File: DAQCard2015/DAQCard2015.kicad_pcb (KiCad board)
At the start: 4 copper layers, 160 x 160 mm, 197 parts, among them CON1 BARREL_JACK, P1 QTH-090-01-F-D-A, P2 QTH-090-01-F-D-A, P3 miniDIL20, P4 LEMO_EPY.00.250.NTN, P5 LEMO_EPY.00.250.NTN, P6 FAN, P7 CONN_02X20_Double, Q1 Q_NPN_BCE, SW1 SPST, U1 RJ45x8, U10 AD9219, U11 THS4524IDBTR, U12 AD9219, U13 THS4524IDBTR, U14 AD9219, U15 THS4524IDBTR, U16 AD9219, U17 THS4524IDBTR, U18 AD9219, U19 CDBHD240-G, U2 AD5628, U20 LM1086, U21 APXS002A0X-SRZ, U22 APXS002A0X-SRZ, U23 APXS002A0X-SRZ, U24 MCP65R41, U3 THS4524IDBTR, U4 AD9219, U5 THS4524IDBTR, U6 AD9219, U7 THS4524IDBTR, U8 AD9219, U9 THS4524IDBTR

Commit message: Various updates to DAQ board focusing on power system
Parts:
- removed C60, C61: 10uF, Capacitors_SMD:C_0805
- removed C62, C63: 10000pF, Capacitors_SMD:C_0603
- removed C64: 3900pF, Capacitors_SMD:C_0603
- removed C65, C66, C67, C68, C69: 47uF, extras:SMD_Cap_8mmDia
- removed REF** (x4): MountingHole_2-5mm, Mounting_Holes:MountingHole_2-5mm
- removed U19: CDBHD240-G, extras:mini-DIP4
- removed U22, U23: APXS002A0X-SRZ, extras:APXS002A0X-SRZ
- added C70: 22nF, Capacitors_SMD:C_1812, F.Cu at (54.1, 150.8)
- added D2: D, Diodes_SMD:SMA_Standard, F.Cu at (51.2, 159.3)
- added D4: MBRA340, Diodes_SMD:SMA_Standard, F.Cu at (151.8, 157.5)
- added DB1: NMLU1210, extras:NMLU1210, F.Cu at (152.8, 167.4)
- added K1: 1462042-8, extras:1462042-8, F.Cu at (54.4, 160.4)
- added L1: 5.6uH, extras:SLF101, F.Cu at (138.8, 152.3)
- added P9: SHV, extras:TE_1217133-1, F.Cu at (58.0, 160.8)
- added Q2: NPN, Housings_SOT-23_SOT-143_TSOT-6:SOT-23, F.Cu at (59.3, 162.7)
- C53: value 100uF -> 22uF
- C55: value 10uF -> 680pF; footprint Capacitors_SMD:C_0805 -> Capacitors_SMD:C_0603
- C56: value 100uF -> 0.47uF; footprint extras:SMD_Cap_8mmDia -> Capacitors_SMD:C_0603
- C57: value 100uF -> 47uF
- C58: value 100uF -> 10uF; footprint extras:SMD_Cap_8mmDia -> Capacitors_SMD:C_0805
- C59: value 10uF -> .1uF; footprint Capacitors_SMD:C_0805 -> Capacitors_SMD:C_0603
- D1: value LED -> Dialight_5690101372F; footprint LEDs:LED-1206 -> extras:Dialight_5690101372F
- R46: value 150R -> 63.4k
- R47: value 5k -> 15k
- R48: value 150R -> 100k
- R49: value 5k -> 536k
- R50: value 220R -> R
- R51: value 2.22k -> R
- R52: value 150R -> R
- R57, R58, R59, R60: footprint Resistors_SMD:R_0603 -> Resistors_SMD:R_1206
- SW1: value SPST -> DPDT
- U11, U13, U15, U17, U3, U5, U7, U9: footprint Housings_SSOP:TSSOP-38_4.4x9.7mm_Pitch0.5mm -> extras:TSSOP-38_4.4x9.7mm_Pitch0.5mm
- U2: footprint Housings_SSOP:TSSOP-16_4.4x5mm_Pitch0.65mm -> extras:TSSOP-16_4.4x5mm_Pitch0.65mm
- U21: value APXS002A0X-SRZ -> LT1913; footprint extras:APXS002A0X-SRZ -> extras:LT1913
- moved R2 282.4 mm to (23.1, 79.9), turned to 270 degrees
- moved R5 276.5 mm to (23.5, 115.8), turned to 270 degrees
- moved R1 265.8 mm to (25.3, 79.9), turned to 90 degrees
- moved C3 263.2 mm to (24.3, 76.9), turned to 180 degrees
- moved C2 256.9 mm to (24.2, 82.9), turned to 180 degrees
- moved C1 249.9 mm to (24.1, 85.7), turned to 180 degrees
- moved R52 235.1 mm to (50.2, 172.4)
- moved D1 231.9 mm to (44.7, 174.3), turned to 180 degrees
- moved R51 199.6 mm to (49.1, 181.5)
- moved R50 194.1 mm to (50.0, 175.3)
- moved R4 189.7 mm to (26.4, 114.4)
- moved C4 180.2 mm to (26.5, 117.3)
- moved C55 142.8 mm to (144.8, 141.5), turned to 180 degrees
- moved C53 142.1 mm to (143.6, 165.6)
- moved RV1 127.4 mm to (157.3, 120.0), turned to 90 degrees
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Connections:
- C55 pad 1: 5Vdig -> Net-(C55-Pad1)
- C56 pad 1: 5Vdig -> Net-(C56-Pad1)
- C56 pad 2: GNDdig -> Net-(C56-Pad2)
- C57 pad 2: GNDdig -> GND
- C58 pad 1: 5Vdig -> 1V8ana
- C58 pad 2: GNDdig -> GND
- C59 pad 1: 5Vdig -> 1V8ana
- C59 pad 2: GNDdig -> GND
- CON1 pad 1: Net-(CON1-Pad1) -> (no net)
- P1 pad 101: /ZEM4310/+3.3VDD -> 3V3dig
- P1 pad 107: /ZEM4310/+3.3VDD -> 3V3dig
- P1 pad 113: /ZEM4310/+3.3VDD -> 3V3dig
- P1 pad 119: /ZEM4310/+3.3VDD -> 3V3dig
- P1 pad 12: (no net) -> 1V8dig
- P1 pad 125: /ZEM4310/+3.3VDD -> 3V3dig
- P1 pad 131: /ZEM4310/+3.3VDD -> 3V3dig
- P1 pad 137: /ZEM4310/+3.3VDD -> 3V3dig
- P1 pad 143: /ZEM4310/+3.3VDD -> 3V3dig
- P1 pad 149: /ZEM4310/+3.3VDD -> 3V3dig
- P1 pad 155: /ZEM4310/+3.3VDD -> 3V3dig
- P1 pad 161: /ZEM4310/+3.3VDD -> 3V3dig
- P1 pad 167: /ZEM4310/+3.3VDD -> 3V3dig
- P1 pad 173: /ZEM4310/+3.3VDD -> 3V3dig
- P1 pad 179: /ZEM4310/+3.3VDD -> 3V3dig
- P1 pad 180: /ZEM4310/PRSNTn -> GND
- P1 pad 65: /ZEM4310/+3.3VDD -> 3V3dig
- P1 pad 71: /ZEM4310/+3.3VDD -> 3V3dig
- P1 pad 77: /ZEM4310/+3.3VDD -> 3V3dig
- P1 pad 83: /ZEM4310/+3.3VDD -> 3V3dig
- P1 pad 89: /ZEM4310/+3.3VDD -> 3V3dig
- P1 pad 95: /ZEM4310/+3.3VDD -> 3V3dig
- P2 pad 101: /ZEM4310/+3.3VDD -> 3V3dig
- P2 pad 107: /ZEM4310/+3.3VDD -> 3V3dig
- P2 pad 11: /ZEM4310/+VDC -> 5Vdig
- P2 pad 113: /ZEM4310/+3.3VDD -> 3V3dig
- P2 pad 119: /ZEM4310/+3.3VDD -> 3V3dig
- P2 pad 12: /ZEM4310/+VDC -> 5Vdig
- P2 pad 125: /ZEM4310/+3.3VDD -> 3V3dig
- P2 pad 131: /ZEM4310/+3.3VDD -> 3V3dig
- P2 pad 137: /ZEM4310/+3.3VDD -> 3V3dig
- P2 pad 143: /ZEM4310/+3.3VDD -> 3V3dig
- P2 pad 149: /ZEM4310/+3.3VDD -> 3V3dig
- P2 pad 155: /ZEM4310/+3.3VDD -> 3V3dig
- P2 pad 161: /ZEM4310/+3.3VDD -> 3V3dig
- P2 pad 167: /ZEM4310/+3.3VDD -> 3V3dig
- P2 pad 173: /ZEM4310/+3.3VDD -> 3V3dig
- P2 pad 179: /ZEM4310/+3.3VDD -> 3V3dig
- P2 pad 180: /ZEM4310/PRSNTn -> GND
- P2 pad 5: /ZEM4310/+VDC -> 5Vdig
- P2 pad 6: /ZEM4310/+VDC -> 5Vdig
- P2 pad 65: /ZEM4310/+3.3VDD -> 3V3dig
- P2 pad 71: /ZEM4310/+3.3VDD -> 3V3dig
- P2 pad 77: /ZEM4310/+3.3VDD -> 3V3dig
- P2 pad 83: /ZEM4310/+3.3VDD -> 3V3dig
- P2 pad 89: /ZEM4310/+3.3VDD -> 3V3dig
- P2 pad 95: /ZEM4310/+3.3VDD -> 3V3dig
- R46 pad 1: 1V8dig -> Net-(R46-Pad1)
- R46 pad 2: Net-(C62-Pad2) -> GND
- R47 pad 1: GNDdig -> Net-(R47-Pad1)
- R47 pad 2: Net-(C62-Pad1) -> Net-(C55-Pad1)
- R48 pad 1: 1V8ana -> Net-(R48-Pad1)
- R48 pad 2: Net-(C63-Pad2) -> GND
- R49 pad 1: GNDdig -> 5Vdig
- R49 pad 2: Net-(C63-Pad1) -> Net-(R48-Pad1)
- R50 pad 1: 3V3dig -> 5Vdig
- R50 pad 2: Net-(C64-Pad2) -> Net-(D1-Pad4)
- R51 pad 1: GNDdig -> HV_control
- R51 pad 2: Net-(C64-Pad1) -> Net-(D1-Pad2)
- R52 pad 1: 5Vdig -> (no net)
- R52 pad 2: Net-(D1-Pad2) -> Net-(D1-Pad5)
- R57 pad 2: (no net) -> GND
- R58 pad 2: (no net) -> /MISCIO/Vbias
- R59 pad 1: (no net) -> Net-(K1-Pad7)
- R60 pad 1: (no net) -> Net-(K1-Pad3)
- R61 pad 1: /MISCIO/HV_control -> HV_control
- R61 pad 2: (no net) -> Net-(Q2-Pad1)
- R62 pad 2: /MISCIO/HV_control -> Net-(D1-Pad7)
- SW1 pad 2: Net-(CON1-Pad1) -> (no net)
- U20 pad 2: 5Vdig -> 1V8ana
- U20 pad 3: Net-(C53-Pad1) -> 5Vdig
- U20 pad 4: 5Vdig -> 1V8ana
- U21 pad 1: (no net) -> 5Vdig
- U21 pad 10: (no net) -> Net-(R46-Pad1)
- U21 pad 2: 5Vdig -> Net-(C56-Pad1)
- U21 pad 3: GNDdig -> Net-(C56-Pad2)
- U21 pad 4: 1V8dig -> Net-(C53-Pad1)
- U21 pad 5: 1V8dig -> Net-(C53-Pad1)
- U21 pad 6: Net-(C62-Pad1) -> GND
- U21 pad 7: GNDdig -> (no net)
- U21 pad 8: (no net) -> Net-(R48-Pad1)
- U21 pad 9: (no net) -> Net-(R47-Pad1)
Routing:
- net /Frontend/ADCChannel8/ADC_Vref: track 11.0 -> 198.8 mm, vias 1 -> 2
- net /Frontend/ADCChannel7/ADC_Vref: track 11.0 -> 172.9 mm, vias 1 -> 2
- net /Frontend/ADCChannel6/ADC_Vref: track 11.0 -> 158.8 mm, vias 1 -> 2
- net /Frontend/ADCChannel5/ADC_Vref: track 11.0 -> 132.8 mm, vias 1 -> 2
- net /Frontend/ADCChannel4/ADC_Vref: track 11.0 -> 118.7 mm, vias 1 -> 2
- net /Frontend/ADCChannel3/ADC_Vref: track 4.39 -> 92.8 mm, vias 1 -> 2
- net /Frontend/ADCChannel2/ADC_Vref: track 4.39 -> 79.1 mm, vias 1 -> 2
- net /Frontend/ADCChannel1/ADC_Vref: track 11.0 -> 53.3 mm, vias 1 -> 2
- net 5Vdig: track 0.00 -> 38.4 mm, vias 0 -> 2
- net Net-(C56-Pad2): track 0.00 -> 23.3 mm
- net Net-(C53-Pad1): track 0.00 -> 14.1 mm
- net GND: track 0.00 -> 10.4 mm
- net Net-(R48-Pad1): track 0.00 -> 7.20 mm
- net 3V3ana: track 28.1 -> 33.3 mm
- net Net-(R47-Pad1): track 0.00 -> 4.71 mm
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- added copper zone on F.Cu, net GND

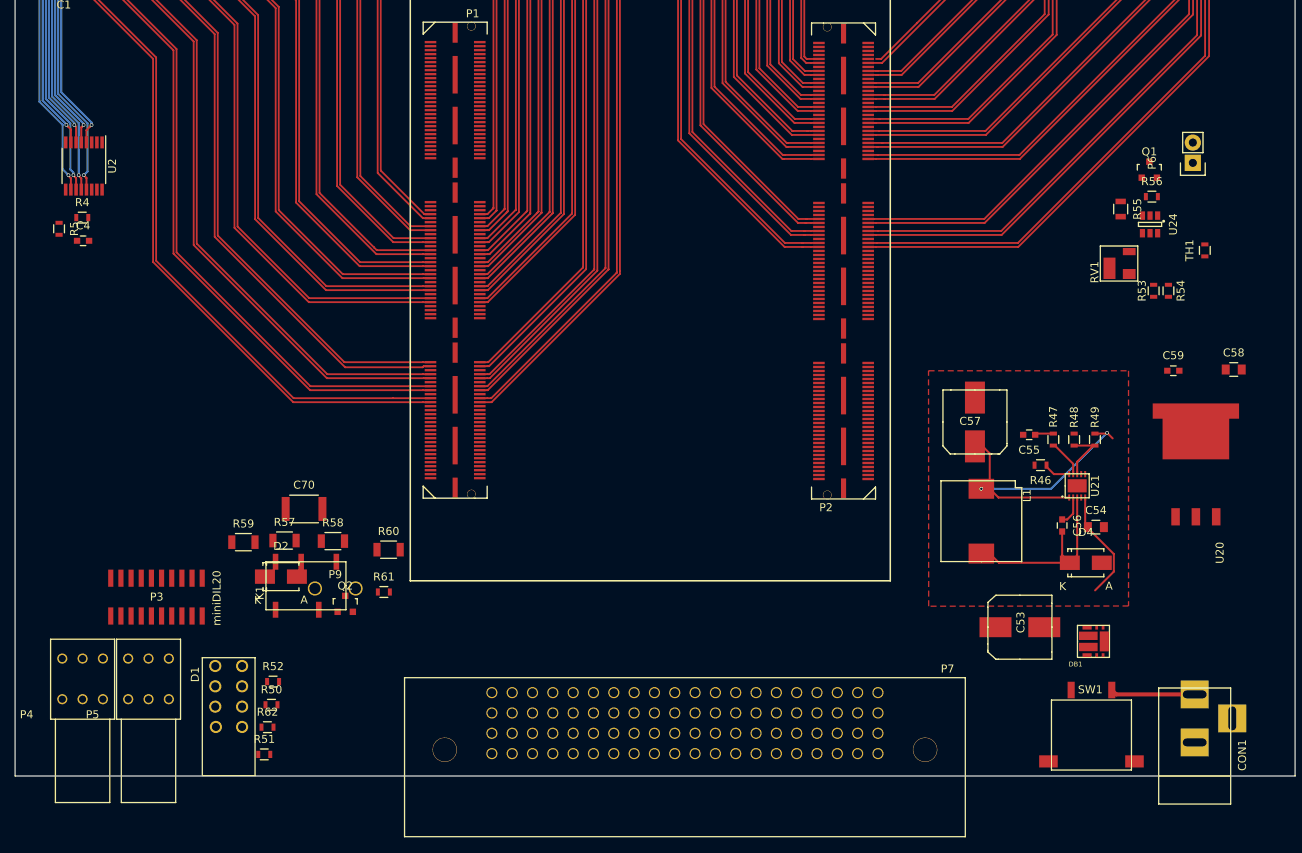
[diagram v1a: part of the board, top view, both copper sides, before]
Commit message: Updates to DAQ Board focusing on the power system and flood fills for it
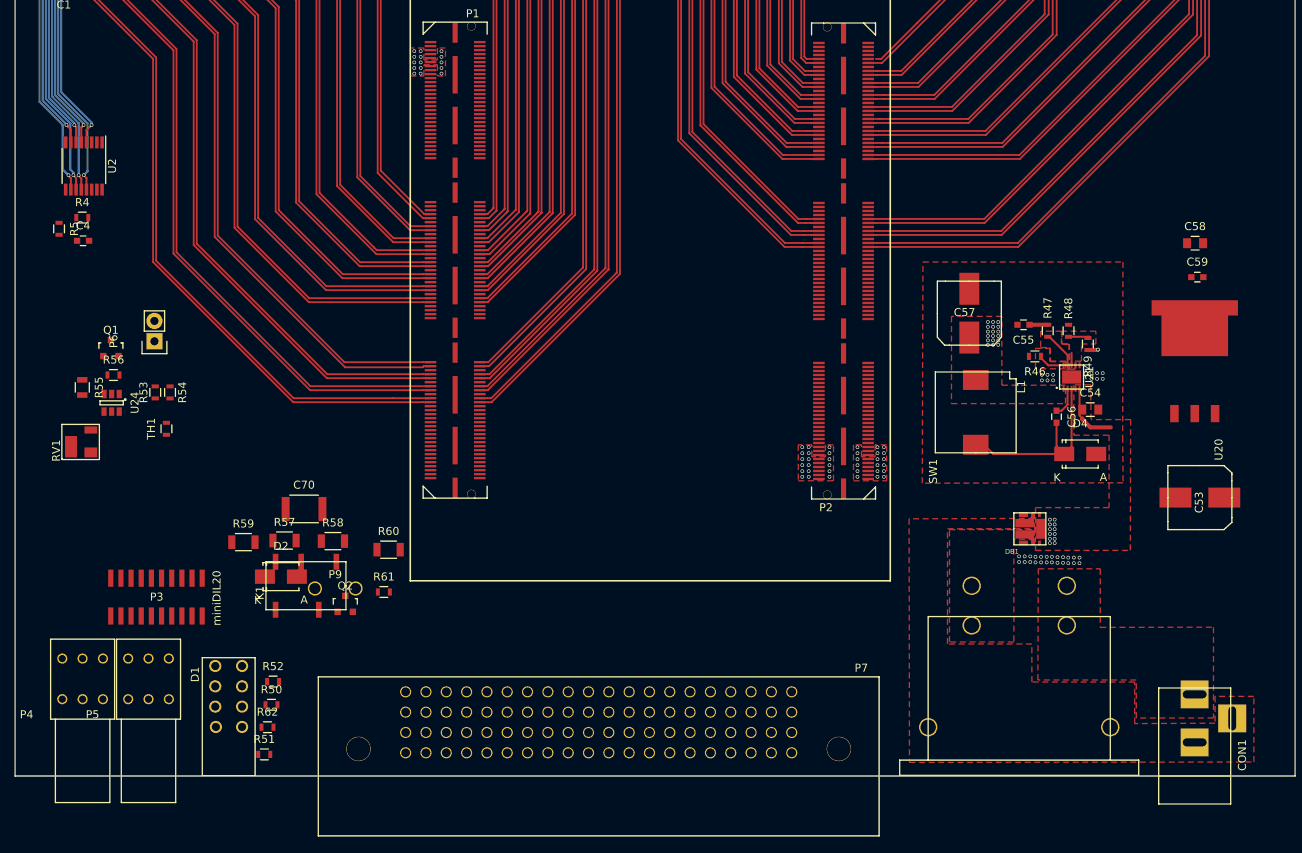
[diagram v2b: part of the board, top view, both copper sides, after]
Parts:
- SW1: footprint extras:Switch_ES02MSABE -> extras:DFXX-XX-X-XX-A-X-XX
- moved P6 131.7 mm to (35.4, 129.9)
- moved Q1 131.7 mm to (30.0, 130.7)
- moved RV1 131.7 mm to (27.5, 142.3)
- moved TH1 131.7 mm to (36.9, 140.8)
- moved U24 131.7 mm to (30.1, 137.6)
- moved R55 131.7 mm to (26.4, 135.6)
- moved R56 131.7 mm to (30.3, 134.1)
- moved R53 125.4 mm to (35.5, 136.2)
- moved R54 125.4 mm to (37.4, 136.2)
- moved C53 27.7 mm to (166.1, 149.4), turned to 270 degrees
- moved C58 16.5 mm to (165.5, 117.6)
- moved DB1 16.2 mm to (144.8, 153.3)
- moved C54 14.7 mm to (152.4, 138.4)
- moved C55 13.8 mm to (144.1, 127.8)
- moved D4 13.6 mm to (151.1, 143.9)
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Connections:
- net /Frontend/Vana renamed Vana
- C11 pad 2: /Frontend/ADC_CLK- -> ADC_CLK-
- C12 pad 2: /Frontend/ADC_CLK+ -> ADC_CLK+
- C17 pad 2: /Frontend/ADC_CLK- -> ADC_CLK-
- C18 pad 2: /Frontend/ADC_CLK+ -> ADC_CLK+
- C23 pad 2: /Frontend/ADC_CLK- -> ADC_CLK-
- C24 pad 2: /Frontend/ADC_CLK+ -> ADC_CLK+
- C29 pad 2: /Frontend/ADC_CLK- -> ADC_CLK-
- C30 pad 2: /Frontend/ADC_CLK+ -> ADC_CLK+
- C35 pad 2: /Frontend/ADC_CLK- -> ADC_CLK-
- C36 pad 2: /Frontend/ADC_CLK+ -> ADC_CLK+
- C4 pad 2: GNDdig -> GND
- C41 pad 2: /Frontend/ADC_CLK- -> ADC_CLK-
- C42 pad 2: /Frontend/ADC_CLK+ -> ADC_CLK+
- C47 pad 2: /Frontend/ADC_CLK- -> ADC_CLK-
- C48 pad 2: /Frontend/ADC_CLK+ -> ADC_CLK+
- C5 pad 2: /Frontend/ADC_CLK- -> ADC_CLK-
- C6 pad 2: /Frontend/ADC_CLK+ -> ADC_CLK+
- CON1 pad 1: (no net) -> Net-(CON1-Pad1)
- R3 pad 1: /Frontend/ADC_CLK- -> ADC_CLK+
- R3 pad 2: /Frontend/ADC_CLK+ -> ADC_CLK-
- R5 pad 1: GNDdig -> GND
- SW1 pad 2: (no net) -> Net-(DB1-Pad4)
- U10 pad 28: /Frontend/ADC_SCLK -> SPI_SCLK
- U10 pad 29: /Frontend/ADC_SDIO -> SPI_SDIO
- U12 pad 28: /Frontend/ADC_SCLK -> SPI_SCLK
- U12 pad 29: /Frontend/ADC_SDIO -> SPI_SDIO
- U14 pad 28: /Frontend/ADC_SCLK -> SPI_SCLK
- U14 pad 29: /Frontend/ADC_SDIO -> SPI_SDIO
- U16 pad 28: /Frontend/ADC_SCLK -> SPI_SCLK
- U16 pad 29: /Frontend/ADC_SDIO -> SPI_SDIO
- U18 pad 28: /Frontend/ADC_SCLK -> SPI_SCLK
- U18 pad 29: /Frontend/ADC_SDIO -> SPI_SDIO
- U2 pad 1: GNDdig -> GND
- U2 pad 14: GNDdig -> GND
- U2 pad 15: /Frontend/ADC_SDIO -> (no net)
- U2 pad 16: /Frontend/ADC_SCLK -> (no net)
- U2 pad 9: GNDdig -> GND
- U4 pad 28: /Frontend/ADC_SCLK -> SPI_SCLK
- U4 pad 29: /Frontend/ADC_SDIO -> SPI_SDIO
- U6 pad 28: /Frontend/ADC_SCLK -> SPI_SCLK
- U6 pad 29: /Frontend/ADC_SDIO -> SPI_SDIO
- U8 pad 28: /Frontend/ADC_SCLK -> SPI_SCLK
- U8 pad 29: /Frontend/ADC_SDIO -> SPI_SDIO
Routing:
- net 5Vdig: track 38.4 -> 1.64 mm, vias 2 -> 1
- net (no net): track 14.4 -> 4.02 mm, vias 0 -> 105
- net Net-(C53-Pad1): track 14.1 -> 7.95 mm, vias 0 -> 12
- net Net-(R48-Pad1): track 7.20 -> 4.35 mm
- net Net-(CON1-Pad2): track 0.00 -> 1.71 mm
- net Net-(DB1-Pad4): track 0.00 -> 1.71 mm
- net GND: track 10.4 -> 11.4 mm
- added copper zone on F.Cu, net 1V8dig
- added copper zone on F.Cu, net 5Vdig
- added copper zone on POWER.Cu, net 5Vdig
- added copper zone on F.Cu, net Net-(C53-Pad1)
- added copper zone on F.Cu, net Net-(CON1-Pad1)
- added copper zone on F.Cu, net Net-(CON1-Pad2)
- added copper zone on F.Cu, net Net-(DB1-Pad4)
- added copper zone on F.Cu, net Net-(R46-Pad1)
- added copper zone on F.Cu, net Net-(R47-Pad1)
- added copper zone on F.Cu, net Net-(R48-Pad1)
